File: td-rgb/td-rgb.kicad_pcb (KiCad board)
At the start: 2 copper layers, 65 x 29 mm, 26 parts, among them J1 ICD15S13E4GV00LF, J2 Conn_01x05_Male, J3 Conn_01x05_Male, J4 Conn_01x02_Male, SW1 SW_DPDT_x2, U1 LT1675CGNPBF, U2 LM2776

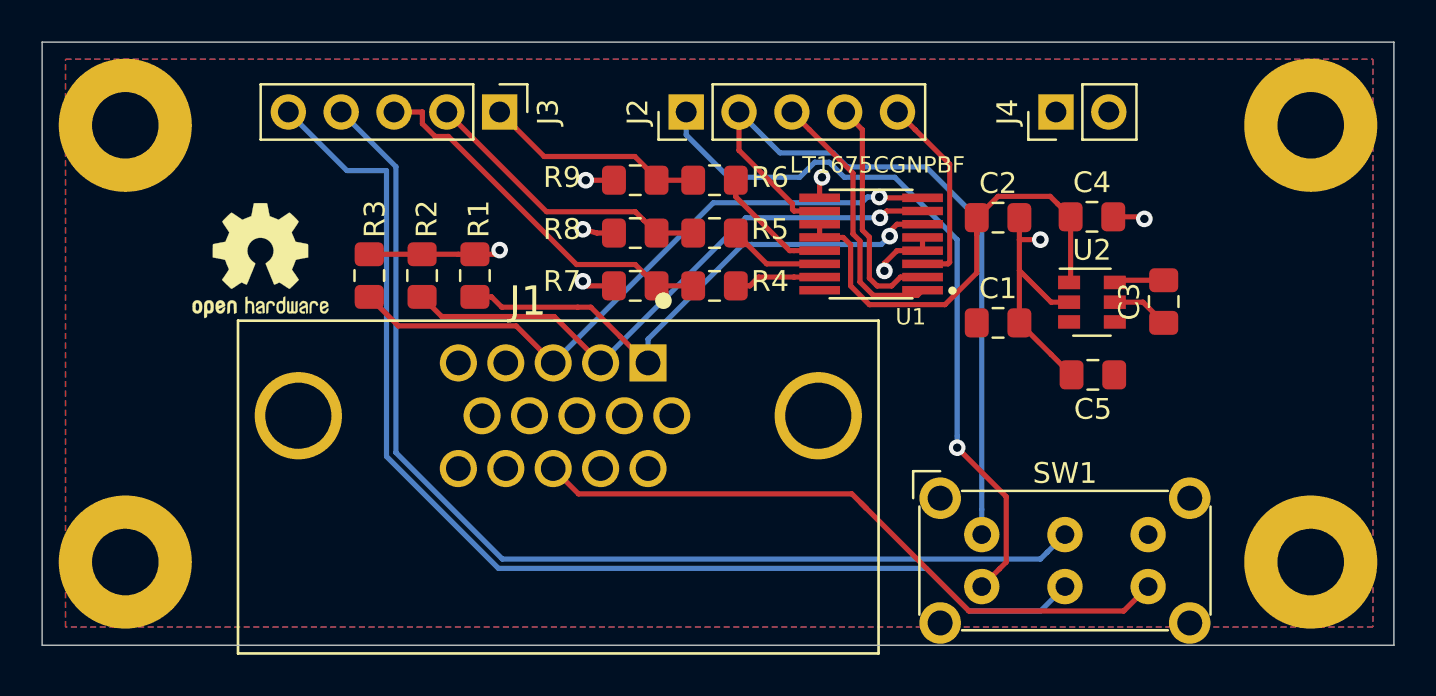
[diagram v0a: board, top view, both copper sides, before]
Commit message: Reverse pin numbering of output header to match input header, connect VGA pin 10 to ground
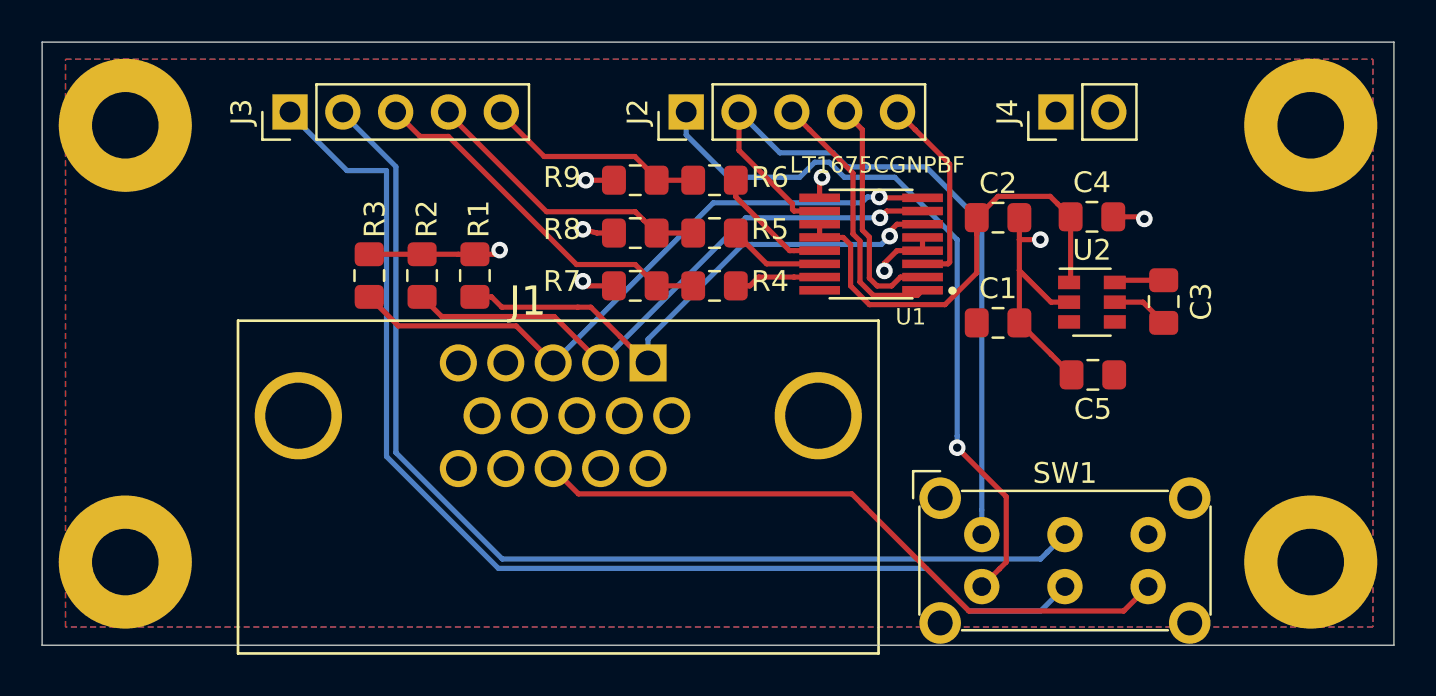
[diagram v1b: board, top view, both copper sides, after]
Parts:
- removed the REF** at (120.5, 93.5)
- C1, C2: value C -> 0.1uF
- U1: footprint LT1675CGNPBF:SOP63P600X172-16N -> SOP63P600X172-16N
- moved J3 10.1 mm to (121.9, 86.4), turned to 90 degrees
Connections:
- J1 pad 10: Net-(J1-Pad10) -> GND
- J3 pad 1: /blue_out -> /csync_out
- J3 pad 2: /green_out -> Net-(J3-Pad2)
- J3 pad 4: Net-(J3-Pad4) -> /green_out
- J3 pad 5: /csync_out -> /blue_out
- SW1 pad 2: Net-(J3-Pad4) -> Net-(J3-Pad2)
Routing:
- net Net-(J3-Pad4): track 52.2 -> 0.00 mm
- net Net-(J3-Pad2): track 0.00 -> 52.2 mm

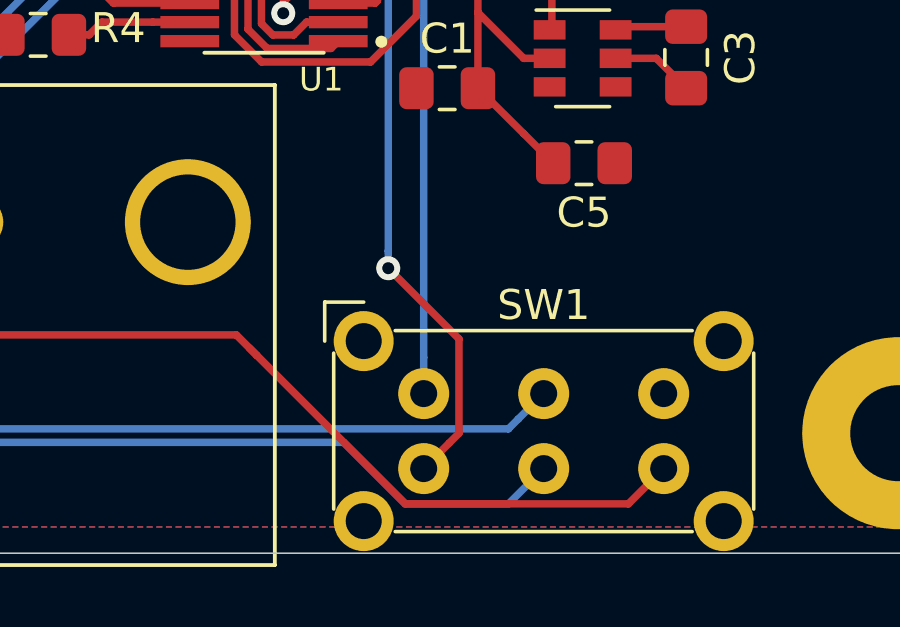
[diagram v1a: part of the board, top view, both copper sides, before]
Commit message: Add series resistor to sync line from VGA (creating voltage divider when terminated into 75ohm at TV's composite video entry point) to attenuate TTL sync signals to video level
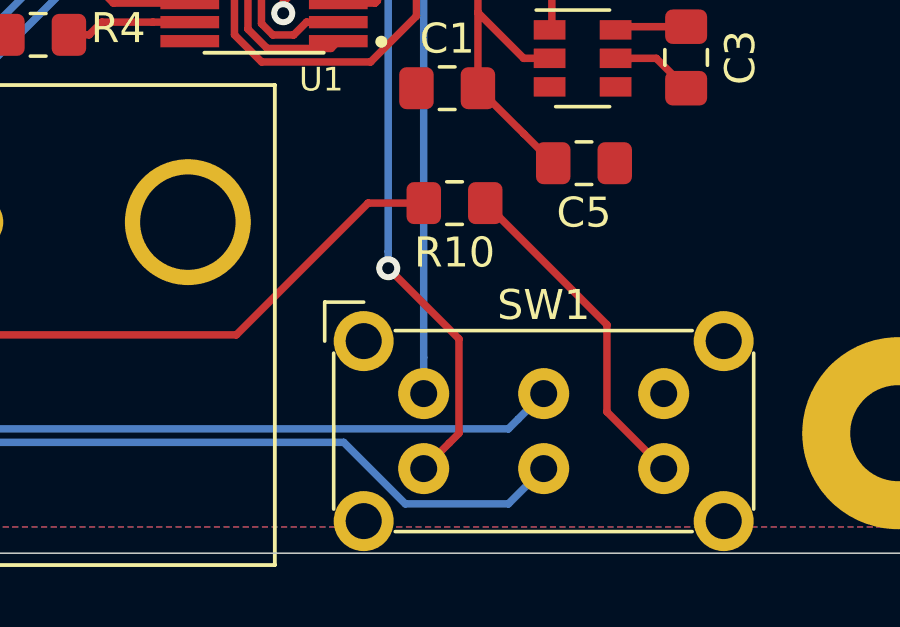
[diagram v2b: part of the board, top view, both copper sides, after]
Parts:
- added R10: 470, Resistor_SMD:R_0805_2012Metric_Pad1.15x1.40mm_HandSolder, F.Cu at (156.2, 100.3)
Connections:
- SW1 pad 6: Net-(J1-Pad13) -> Net-(R10-Pad1)
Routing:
- net Net-(R10-Pad1): track 0.00 -> 11.3 mm
- net Net-(J1-Pad13): track 32.3 -> 22.9 mm
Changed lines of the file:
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@@
     (tracks 184)
     (zones 0)
-    (modules 25)
-    (nets 29)
+    (modules 26)
+    (nets 30)
   )
   (page A4)
@@
   (net 27 /blank_in)
   (net 28 "Net-(J3-Pad2)")
+  (net 29 "Net-(R10-Pad1)")
   (net_class Default "This is the default net class."
     (clearance 0.2)
@@
     (add_net "Net-(J2-Pad1)")
     (add_net "Net-(J3-Pad2)")
+    (add_net "Net-(R10-Pad1)")
     (add_net "Net-(R4-Pad2)")
     (add_net "Net-(R5-Pad2)")
     (add_net "Net-(R6-Pad2)")
+  )
+  (module Resistor_SMD:R_0805_2012Metric_Pad1.15x1.40mm_HandSolder (layer F.Cu)
+    (at 156.21 100.33 180)
+    (descr "Resistor SMD 0805 (2012 Metric), square (rectangular) end terminal, IPC_7351 nominal with elongated pad for handsoldering. (Body size source: https://docs.google.com/spreadsheets/d/1BsfQQcO9C6DZCsRaXUlFlo91Tg2WpOkGARC1WS5S8t0/edit?usp=sharing), generated with kicad-footprint-generator")
+    (tags "resistor handsolder")
+    (attr smd)
+    (fp_text reference R10 (at 0 -1.65 180) (layer F.SilkS)
+      (effects (font (size 1 1) (thickness 0.15)))
+    )
+    (fp_text value 470 (at 0 1.65 180) (layer F.Fab)
+      (effects (font (size 1 1) (thickness 0.15)))
+    )
+    (fp_line (start -1 0.6) (end -1 -0.6) (layer F.Fab) (width 0.1))
+    (fp_line (start -1 -0.6) (end 1 -0.6) (layer F.Fab) (width 0.1))
+    (fp_line (start 1 -0.6) (end 1 0.6) (layer F.Fab) (width 0.1))
+    (fp_line (start 1 0.6) (end -1 0.6) (layer F.Fab) (width 0.1))
+    (fp_line (start -0.261252 -0.71) (end 0.261252 -0.71) (layer F.SilkS) (width 0.12))
+    (fp_line (start -0.261252 0.71) (end 0.261252 0.71) (layer F.SilkS) (width 0.12))
+    (fp_line (start -1.85 0.95) (end -1.85 -0.95) (layer F.CrtYd) (width 0.05))
+    (fp_line (start -1.85 -0.95) (end 1.85 -0.95) (layer F.CrtYd) (width 0.05))
+    (fp_line (start 1.85 -0.95) (end 1.85 0.95) (layer F.CrtYd) (width 0.05))
+    (fp_line (start 1.85 0.95) (end -1.85 0.95) (layer F.CrtYd) (width 0.05))
+    (fp_text user %R (at 0 0 180) (layer F.Fab)
+      (effects (font (size 0.5 0.5) (thickness 0.08)))
+    )
+    (pad 1 smd roundrect (at -1.025 0 180) (size 1.15 1.4) (layers F.Cu F.Paste F.Mask) (roundrect_rratio 0.217391)
+      (net 29 "Net-(R10-Pad1)"))
+    (pad 2 smd roundrect (at 1.025 0 180) (size 1.15 1.4) (layers F.Cu F.Paste F.Mask) (roundrect_rratio 0.217391)
+      (net 6 "Net-(J1-Pad13)"))
+    (model ${KISYS3DMOD}/Resistor_SMD.3dshapes/R_0805_2012Metric.wrl
+      (at (xyz 0 0 0))
+      (scale (xyz 1 1 1))
+      (rotate (xyz 0 0 0))
+    )
   )
   (module 1-1734530-1:TE_1-1734530-1 (layer F.Cu)
@@
     (fp_line (start -3.3 -3.05) (end -2 -3.05) (layer F.SilkS) (width 0.12))
     (pad 6 thru_hole circle (at 8 2.5) (size 1.7 1.7) (drill 0.9) (layers *.Cu *.Mask)
-      (net 6 "Net-(J1-Pad13)"))
+      (net 29 "Net-(R10-Pad1)"))
     (pad 5 thru_hole circle (at 4 2.5) (size 1.7 1.7) (drill 0.9) (layers *.Cu *.Mask)
       (net 15 /csync_out))
@@
   (segment (start 148.52 92.3925) (end 148.874976 92.747476) (width 0.25) (layer F.Cu) (net 3))
   (segment (start 147.385 92.3925) (end 148.52 92.3925) (width 0.25) (layer F.Cu) (net 3))
-  (segment (start 162.007 110.355001) (end 154.568004 110.355001) (width 0.25) (layer F.Cu) (net 6))
-  (segment (start 163.182001 109.18) (end 162.007 110.355001) (width 0.25) (layer F.Cu) (net 6))
-  (segment (start 148.935504 104.722501) (end 149.623003 105.41) (width 0.25) (layer F.Cu) (net 6))
   (segment (start 135.792501 104.722501) (end 148.935504 104.722501) (width 0.25) (layer F.Cu) (net 6))
   (segment (start 134.575 103.505) (end 135.792501 104.722501) (width 0.25) (layer F.Cu) (net 6))
-  (segment (start 154.568004 110.355001) (end 149.623003 105.41) (width 0.25) (layer F.Cu) (net 6))
-  (segment (start 149.623003 105.41) (end 149.370504 105.157501) (width 0.25) (layer F.Cu) (net 6))
+  (segment (start 153.328005 100.33) (end 155.185 100.33) (width 0.25) (layer F.Cu) (net 6))
+  (segment (start 148.935504 104.722501) (end 153.328005 100.33) (width 0.25) (layer F.Cu) (net 6))
   (segment (start 152.335 90.4875) (end 150.291131 90.4875) (width 0.25) (layer F.Cu) (net 11))
   (segment (start 150.291131 90.4875) (end 150.250359 90.446728) (width 0.25) (layer F.Cu) (net 11))
@@
   (segment (start 126.560593 89.177003) (end 124.657002 89.177002) (width 0.25) (layer B.Cu) (net 15))
   (segment (start 126.560594 102.923906) (end 126.560593 89.177003) (width 0.25) (layer B.Cu) (net 15))
-  (segment (start 158.332002 107.529999) (end 159.182001 106.68) (width 0.25) (layer B.Cu) (net 28))
-  (segment (start 158.007 107.855001) (end 158.332002 107.529999) (width 0.25) (layer B.Cu) (net 28))
-  (segment (start 132.128099 107.855001) (end 158.007 107.855001) (width 0.25) (layer B.Cu) (net 28))
-  (segment (start 127.010603 102.737505) (end 132.128099 107.855001) (width 0.25) (layer B.Cu) (net 28))
-  (segment (start 127.010603 88.990603) (end 127.010603 102.737505) (width 0.25) (layer B.Cu) (net 28))
-  (segment (start 124.38 86.36) (end 127.010603 88.990603) (width 0.25) (layer B.Cu) (net 28))
   (segment (start 146.155 94.2975) (end 147.385 94.2975) (width 0.25) (layer F.Cu) (net 16))
   (segment (start 144.454078 94.2975) (end 146.155 94.2975) (width 0.25) (layer F.Cu) (net 16))
@@
   (segment (start 155.182001 105.477919) (end 155.182001 106.68) (width 0.25) (layer B.Cu) (net 27))
   (segment (start 155.182001 91.682001) (end 155.182001 105.477919) (width 0.25) (layer B.Cu) (net 27))
+  (segment (start 158.332002 107.529999) (end 159.182001 106.68) (width 0.25) (layer B.Cu) (net 28))
+  (segment (start 158.007 107.855001) (end 158.332002 107.529999) (width 0.25) (layer B.Cu) (net 28))
+  (segment (start 132.128099 107.855001) (end 158.007 107.855001) (width 0.25) (layer B.Cu) (net 28))
+  (segment (start 127.010603 102.737505) (end 132.128099 107.855001) (width 0.25) (layer B.Cu) (net 28))
+  (segment (start 127.010603 88.990603) (end 127.010603 102.737505) (width 0.25) (layer B.Cu) (net 28))
+  (segment (start 124.38 86.36) (end 127.010603 88.990603) (width 0.25) (layer B.Cu) (net 28))
+  (segment (start 157.235 100.33) (end 161.29 104.385) (width 0.25) (layer F.Cu) (net 29))
+  (segment (start 161.29 107.287999) (end 163.182001 109.18) (width 0.25) (layer F.Cu) (net 29))
+  (segment (start 161.29 104.385) (end 161.29 107.287999) (width 0.25) (layer F.Cu) (net 29))
   (zone (net 1) (net_name GND) (layer B.Cu) (hatch edge 0.508)
     (connect_pads (clearance 0.2))
